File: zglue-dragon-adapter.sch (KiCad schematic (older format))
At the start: 58 parts, among them J1 543630489, J2 543630489, U1 zGlue-Dragon

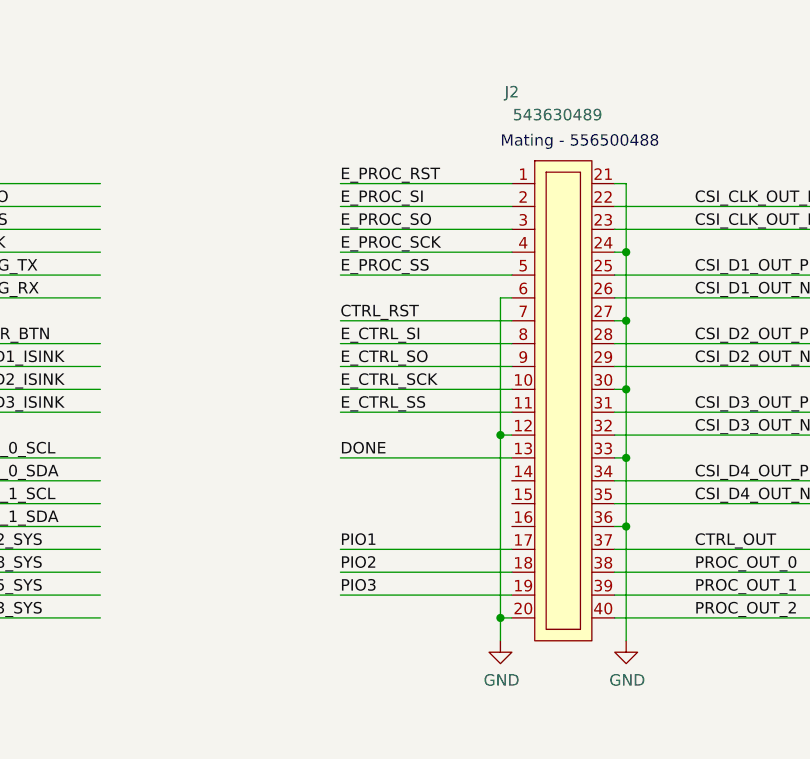
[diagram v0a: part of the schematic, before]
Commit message: Added QSPI flash signals to unify with GEM2 adapter
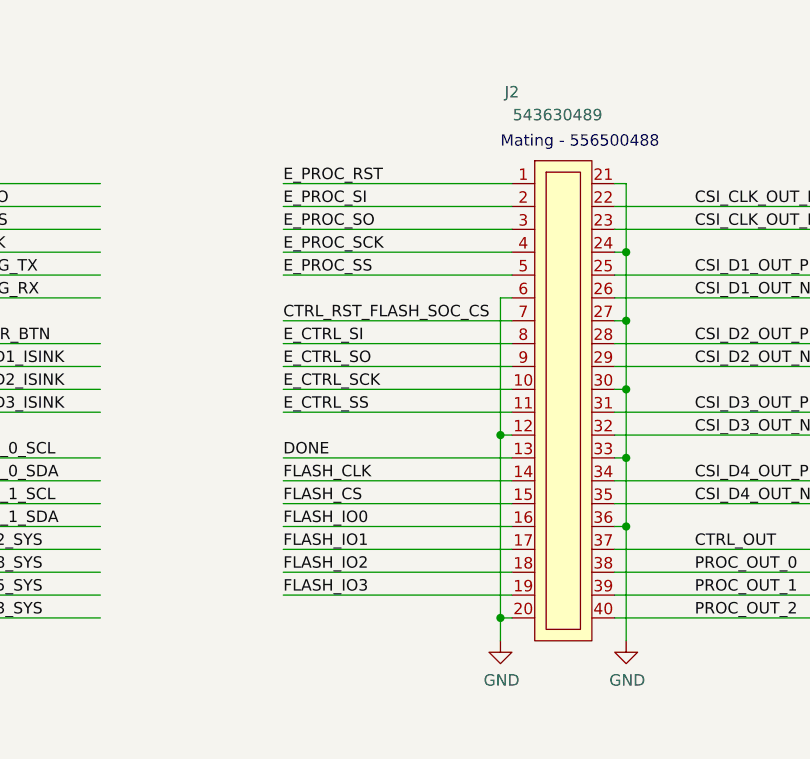
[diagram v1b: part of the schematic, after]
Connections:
- net labels added: CTRL_RST_FLASH_SOC_CS, FLASH_CLK, FLASH_CS, FLASH_IO0, FLASH_IO1, FLASH_IO2, FLASH_IO3
- wire segments 264 -> 267
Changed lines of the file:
@@
 EESchema Schematic File Version 4
+LIBS:zglue-dragon-adapter-cache
 EELAYER 26 0
 EELAYER END
@@
 Text Label 12650 3450 0    50   ~ 0
 PROC_OUT_2
-Text Label 11100 1550 0    50   ~ 0
+Text Label 10850 1550 0    50   ~ 0
 E_PROC_RST
-Text Label 11100 1650 0    50   ~ 0
+Text Label 10850 1650 0    50   ~ 0
 E_PROC_SI
-Text Label 11100 1750 0    50   ~ 0
+Text Label 10850 1750 0    50   ~ 0
 E_PROC_SO
-Text Label 11100 1850 0    50   ~ 0
+Text Label 10850 1850 0    50   ~ 0
 E_PROC_SCK
-Text Label 11100 1950 0    50   ~ 0
+Text Label 10850 1950 0    50   ~ 0
 E_PROC_SS
-Text Label 11100 2150 0    50   ~ 0
-CTRL_RST
+Text Label 10850 2150 0    50   ~ 0
+CTRL_RST_FLASH_SOC_CS
 Text Label 7900 5650 0    50   ~ 0
 CTRL_SI
@@
 Text Label 12650 3150 0    50   ~ 0
 CTRL_OUT
-Text Label 11100 2750 0    50   ~ 0
+Text Label 10850 2750 0    50   ~ 0
 DONE
 Text Label 9850 7950 0    50   ~ 0
@@
 	12300 3450 13200 3450
 Wire Wire Line
-	11850 1550 11100 1550
-Wire Wire Line
-	11850 1650 11100 1650
-Wire Wire Line
-	11850 1750 11100 1750
-Wire Wire Line
-	11850 1850 11100 1850
+	11850 1550 10850 1550
+Wire Wire Line
+	11850 1650 10850 1650
+Wire Wire Line
+	11850 1750 10850 1750
+Wire Wire Line
+	11850 1850 10850 1850
 $Comp
 L power:GND #PWR022
@@
 	11800 2050 11800 2650
 Wire Wire Line
-	11850 1950 11100 1950
+	11850 1950 10850 1950
 Wire Wire Line
 	11850 2050 11800 2050
 Wire Wire Line
-	11850 2150 11100 2150
-Wire Wire Line
-	11850 2250 11100 2250
-Wire Wire Line
-	11850 2350 11100 2350
-Wire Wire Line
-	11850 2450 11100 2450
-Wire Wire Line
-	11850 2550 11100 2550
+	11850 2150 10850 2150
+Wire Wire Line
+	11850 2250 10850 2250
+Wire Wire Line
+	11850 2350 10850 2350
+Wire Wire Line
+	11850 2450 10850 2450
+Wire Wire Line
+	11850 2550 10850 2550
 $Comp
 L antmicroResistors0402:R_0R_0402 R15
@@
 	11800 2650 11800 3450
 Wire Wire Line
-	11850 2750 11100 2750
-Text Label 11100 2250 0    50   ~ 0
+	11850 2750 10850 2750
+Text Label 10850 2250 0    50   ~ 0
 E_CTRL_SI
-Text Label 11100 2350 0    50   ~ 0
+Text Label 10850 2350 0    50   ~ 0
 E_CTRL_SO
-Text Label 11100 2450 0    50   ~ 0
+Text Label 10850 2450 0    50   ~ 0
 E_CTRL_SCK
-Text Label 11100 2550 0    50   ~ 0
+Text Label 10850 2550 0    50   ~ 0
 E_CTRL_SS
 Text Notes 11800 1400 0    50   ~ 0
 Mating - 556500488
-Wire Wire Line
-	11850 3150 11100 3150
-Wire Wire Line
-	11850 3250 11100 3250
-Wire Wire Line
-	11850 3350 11100 3350
 Wire Wire Line
 	11800 3450 11850 3450
@@
 Wire Wire Line
 	8750 6100 9700 6100
-Text Label 11100 3350 0    50   ~ 0
-PIO3
-Text Label 11100 3250 0    50   ~ 0
-PIO2
-Text Label 11100 3150 0    50   ~ 0
-PIO1
 Text Label 1950 2450 0    50   ~ 0
 MIPI_SEL
@@
 Text Label 9500 2550 0    50   ~ 0
 LED3_ISINK
+Text Label 10850 2850 0    50   ~ 0
+FLASH_CLK
+Text Label 10850 2950 0    50   ~ 0
+FLASH_CS
+Text Label 10850 3050 0    50   ~ 0
+FLASH_IO0
+Text Label 10850 3150 0    50   ~ 0
+FLASH_IO1
+Text Label 10850 3250 0    50   ~ 0
+FLASH_IO2
+Wire Wire Line
+	11850 2850 10850 2850
+Wire Wire Line
+	11850 2950 10850 2950
+Wire Wire Line
+	11850 3050 10850 3050
+Wire Wire Line
+	11850 3150 10850 3150
+Wire Wire Line
+	11850 3250 10850 3250
+Text Label 10850 3350 0    50   ~ 0
+FLASH_IO3
+Wire Wire Line
+	11850 3350 10850 3350
 $EndSCHEMATC

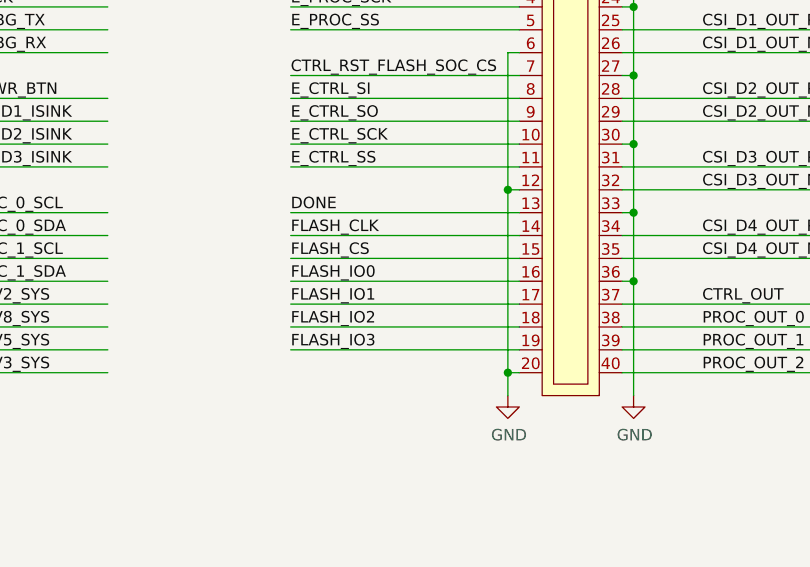
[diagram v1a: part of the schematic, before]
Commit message: QSPI signals marked as reserved
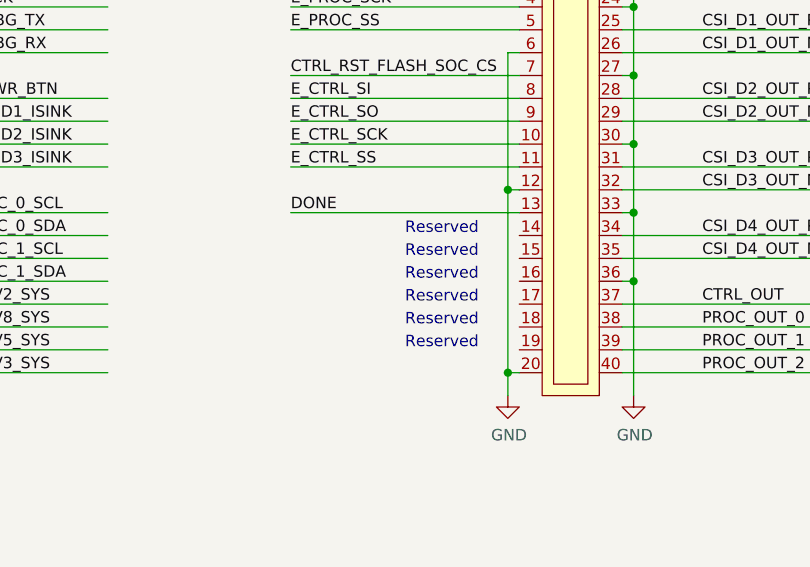
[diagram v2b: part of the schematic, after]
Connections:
- net labels removed: FLASH_CLK, FLASH_CS, FLASH_IO0, FLASH_IO1, FLASH_IO2, FLASH_IO3
- wire segments 267 -> 261
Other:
- note added: "Reserved"
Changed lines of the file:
@@
 EESchema Schematic File Version 4
-LIBS:zglue-dragon-adapter-cache
 EELAYER 26 0
 EELAYER END
@@
 Text Label 9500 2550 0    50   ~ 0
 LED3_ISINK
-Text Label 10850 2850 0    50   ~ 0
-FLASH_CLK
-Text Label 10850 2950 0    50   ~ 0
-FLASH_CS
-Text Label 10850 3050 0    50   ~ 0
-FLASH_IO0
-Text Label 10850 3150 0    50   ~ 0
-FLASH_IO1
-Text Label 10850 3250 0    50   ~ 0
-FLASH_IO2
-Wire Wire Line
-	11850 2850 10850 2850
-Wire Wire Line
-	11850 2950 10850 2950
-Wire Wire Line
-	11850 3050 10850 3050
-Wire Wire Line
-	11850 3150 10850 3150
-Wire Wire Line
-	11850 3250 10850 3250
-Text Label 10850 3350 0    50   ~ 0
-FLASH_IO3
-Wire Wire Line
-	11850 3350 10850 3350
+Text Notes 11350 2850 0    50   ~ 0
+Reserved
+Text Notes 11350 2950 0    50   ~ 0
+Reserved
+Text Notes 11350 3050 0    50   ~ 0
+Reserved
+Text Notes 11350 3150 0    50   ~ 0
+Reserved
+Text Notes 11350 3250 0    50   ~ 0
+Reserved
+Text Notes 11350 3350 0    50   ~ 0
+Reserved
 $EndSCHEMATC

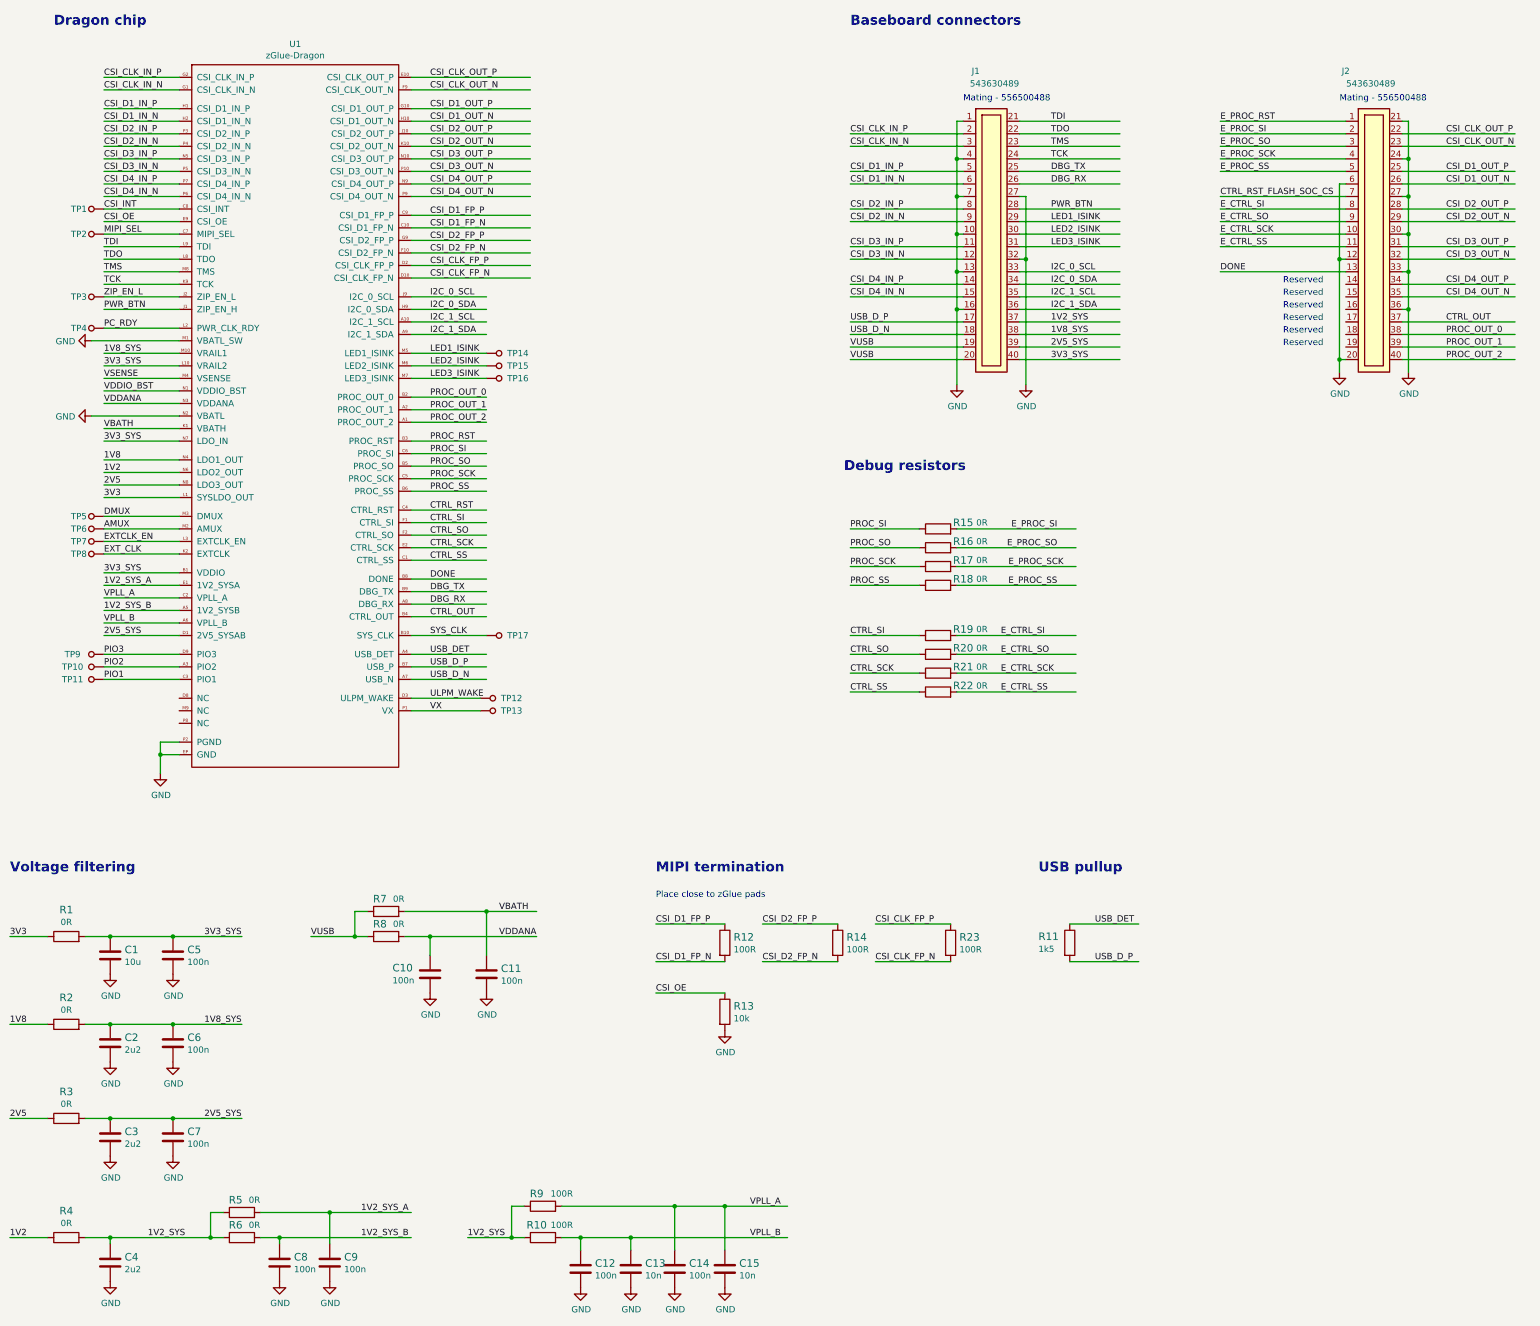
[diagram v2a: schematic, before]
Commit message: Added NC to specified signals from ZiP
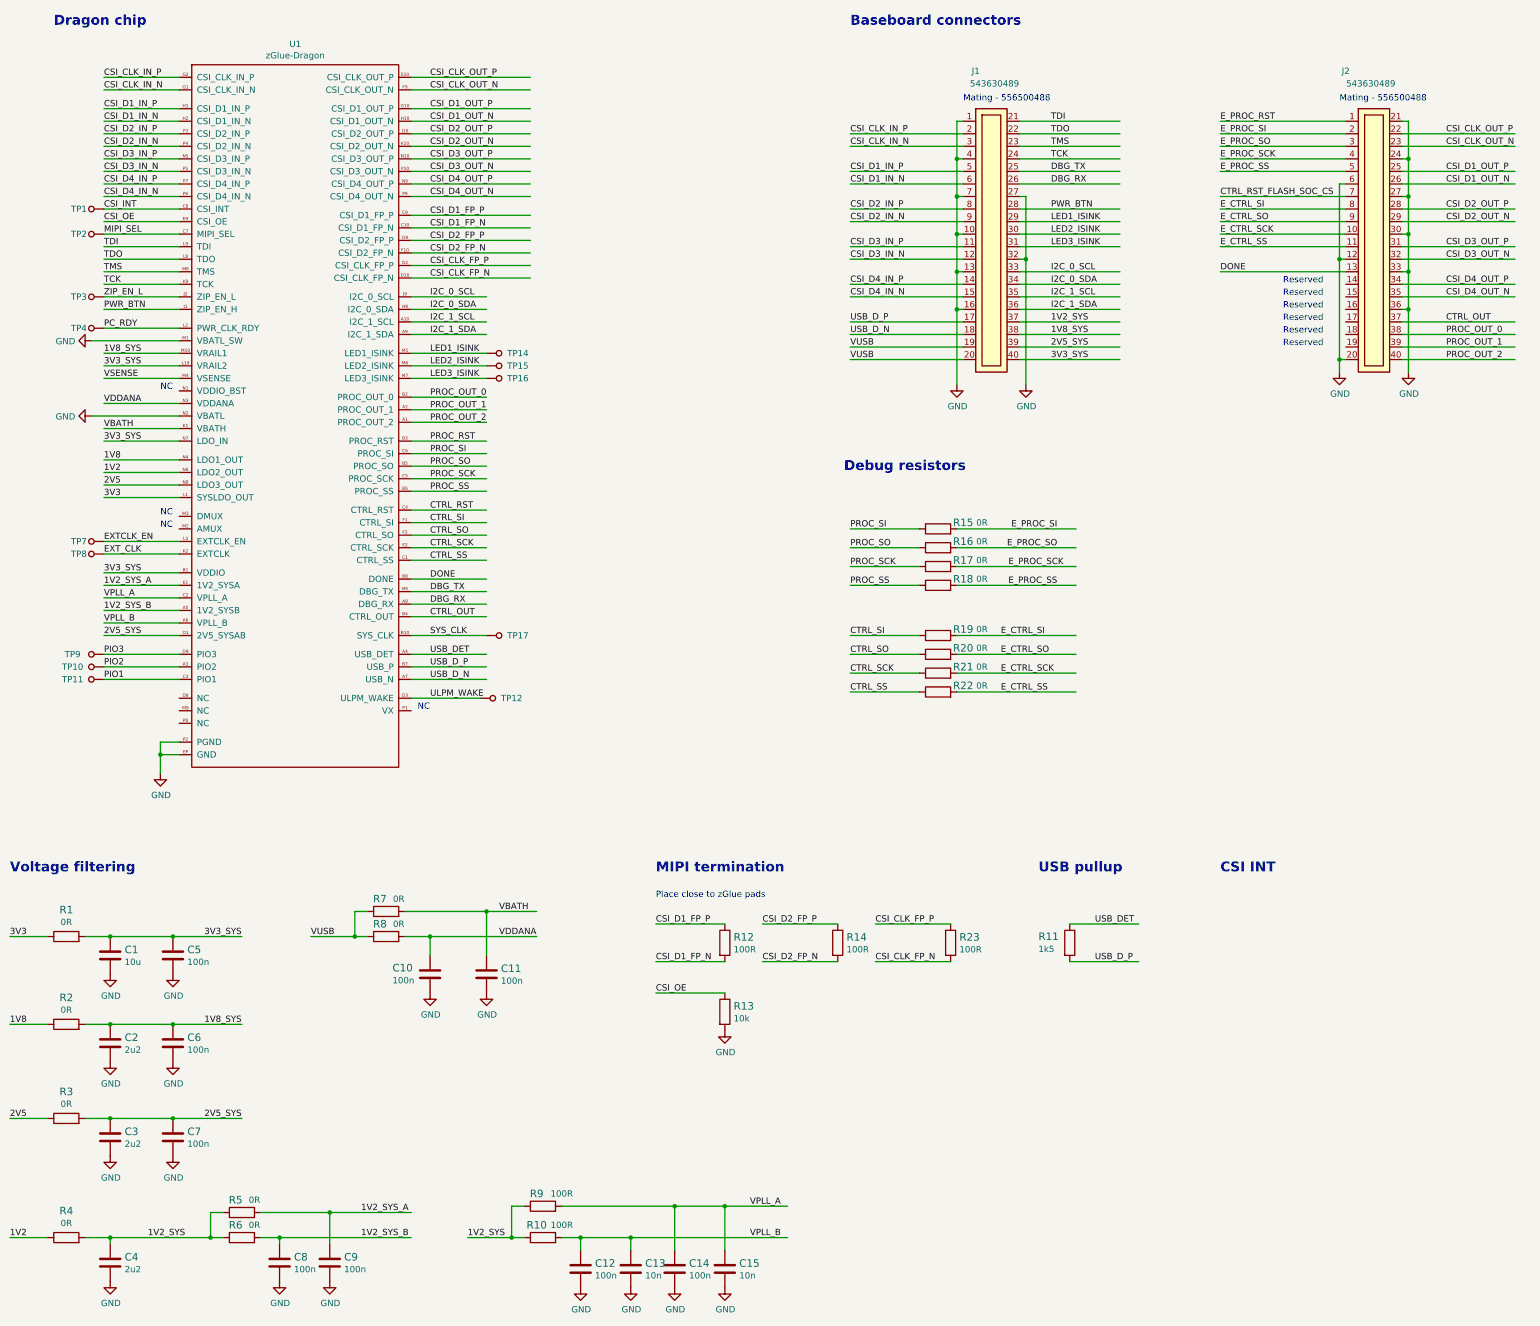
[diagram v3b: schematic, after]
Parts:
- removed TP13, TP5, TP6: TP_SMD1MM, antmicro-footprints:Testpoint_smd_1mm, symbol antmicroTestPoints:TP_SMD1MM
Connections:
- net labels removed: AMUX, DMUX, VDDIO_BST, VX
- wire segments 261 -> 257
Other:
- note added: "CSI INT"
- note added: "NC"
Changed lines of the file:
@@
-$EndComp
-$Comp
-L antmicroTestPoints:TP_SMD1MM TP5
-U 1 1 5D8CA6F0
-P 1850 4700
-F 0 "TP5" V 1850 4600 50  0000 C CNN
-F 1 "TP_SMD1MM" H 1850 4600 50  0001 C CNN
-F 2 "antmicro-footprints:Testpoint_smd_1mm" H 2050 4900 60  0001 L CNN
-F 3 "" H 2050 5000 60  0001 L CNN
-	1    1850 4700
-	0    1    1    0
-$EndComp
-$Comp
-L antmicroTestPoints:TP_SMD1MM TP6
-U 1 1 5D8CA73B
-P 1850 4800
-F 0 "TP6" V 1850 4700 50  0000 C CNN
-F 1 "TP_SMD1MM" H 1850 4700 50  0001 C CNN
-F 2 "antmicro-footprints:Testpoint_smd_1mm" H 2050 5000 60  0001 L CNN
-F 3 "" H 2050 5100 60  0001 L CNN
-	1    1850 4800
-	0    1    1    0
 $EndComp
 $Comp
@@
 	4400 5500 5000 5500
 Wire Wire Line
-	2550 4700 1950 4700
-Wire Wire Line
-	2550 4800 1950 4800
-Text Label 1950 4700 0    50   ~ 0
-DMUX
-Text Label 1950 4800 0    50   ~ 0
-AMUX
-Wire Wire Line
 	2550 4900 1950 4900
 Wire Wire Line
@@
 Wire Wire Line
 	1850 3300 2550 3300
-$Comp
-L antmicroTestPoints:TP_SMD1MM TP13
-U 1 1 5D92F140
-P 5050 6250
-F 0 "TP13" V 5050 6100 50  0000 C CNN
-F 1 "TP_SMD1MM" H 5050 6150 50  0001 C CNN
-F 2 "antmicro-footprints:Testpoint_smd_1mm" H 5250 6450 60  0001 L CNN
-F 3 "" H 5250 6550 60  0001 L CNN
-	1    5050 6250
-	0    -1   -1   0
-$EndComp
-Wire Wire Line
-	4400 6250 4950 6250
 Wire Wire Line
 	4400 6150 4950 6150
@@
 Text Label 4550 6150 0    50   ~ 0
 ULPM_WAKE
-Text Label 4550 6250 0    50   ~ 0
-VX
 $Comp
 L power:GND #PWR07
@@
 Wire Wire Line
 	2550 3600 1950 3600
-Wire Wire Line
-	2550 3700 1950 3700
 Text Label 1950 3600 0    50   ~ 0
 VSENSE
-Text Label 1950 3700 0    50   ~ 0
-VDDIO_BST
 Text Label 1950 5800 0    50   ~ 0
 PIO3
@@
 Text Notes 11350 3350 0    50   ~ 0
 Reserved
+Text Notes 10850 7550 0    79   ~ 16
+CSI INT
+Text Notes 2400 4700 0    50   ~ 0
+NC
+Text Notes 2400 3700 0    50   ~ 0
+NC
+Text Notes 4450 6250 0    50   ~ 0
+NC
+Text Notes 2400 4800 0    50   ~ 0
+NC
 $EndSCHEMATC

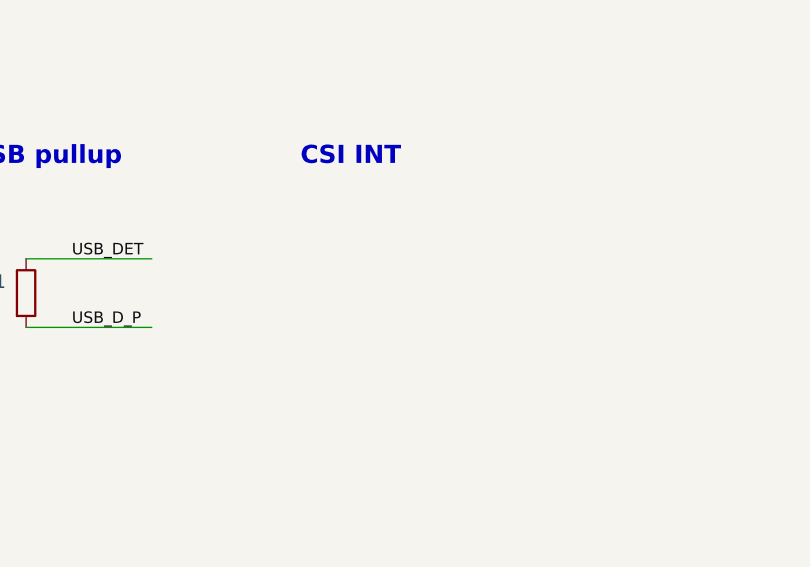
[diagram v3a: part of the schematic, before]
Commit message: Added CSI INT
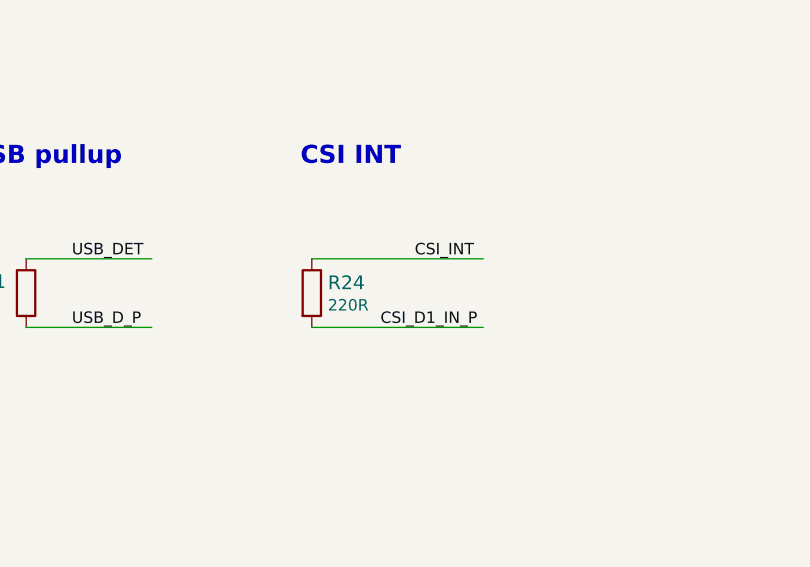
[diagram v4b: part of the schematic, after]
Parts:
- added R24: R_220R_0402, antmicro-footprints:0402-res, symbol antmicroResistors0402:R_220R_0402
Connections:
- wire segments 257 -> 259
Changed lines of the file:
@@
 Text Notes 2400 4800 0    50   ~ 0
 NC
+Wire Wire Line
+	10900 7950 11650 7950
+Text Label 11350 7950 0    50   ~ 0
+CSI_INT
+Text Label 11200 8250 0    50   ~ 0
+CSI_D1_IN_P
+$Comp
+L antmicroResistors0402:R_220R_0402 R24
+U 1 1 5DA2E339
+P 10900 8100
+F 0 "R24" V 10855 8170 60  0000 L CNN
+F 1 "R_220R_0402" H 10900 7950 60  0001 C CNN
+F 2 "antmicro-footprints:0402-res" H 11100 8300 60  0001 L CNN
+F 3 "" H 10900 8100 50  0001 C CNN
+F 4 "TE_CONNECTIVITY_/_NEOHM" H 11100 8500 60  0001 L CNN "Manufacturer"
+F 5 "CRG0402J220R" H 11100 8400 60  0001 L CNN "MPN"
+F 6 "220R" V 10953 8170 50  0000 L CNN "Val"
+	1    10900 8100
+	0    1    1    0
+$EndComp
+Wire Wire Line
+	10900 8250 11650 8250
 $EndSCHEMATC
